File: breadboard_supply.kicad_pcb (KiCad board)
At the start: 4 copper layers, 54 x 100 mm, 187 parts, among them J1 USB_C_Receptacle_USB2.0, J2 Barrel_Jack_Switch, J3 ST-Link, J4 SHDN, J5 SHDN, J6 RAIL_POL, J7 OUTPUT, J8 RAIL_POL, J9 OUTPUT, K1 HFD4-3, K2 HFD4-3, Q1 AO4805, Q2 AO4805, Q3 DMG2302U, Q4 AO4805, Q5 DMG2302U, Q6 DMG2302U, SW1 Button, SW2 Button, SW3 Button, SW4 Button, SW5 Button, U1 USBLC6-2SC6, U10 MAX5400, U11 SL6206-33NR, U12 STM32F070RBT6, U13 GN1640T, U14 74LVC1G14, U15 74LVC1G14, U16 INA180A4, U17 INA180A4, U2 CYPD3177-24LQXQ, U3 DZDH0401DW, U4 INA180A4, U5 DZDH0401DW, U6 TPS54202DDC, U7 TPS54202DDC, U8 MAX5400, U9 TPS54202DDC, Y1 8MHz

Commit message: WIP PCB Routing
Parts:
- L1, L2, L3: footprint Inductor_SMD:L_6.3x6.3_H3 -> Inductor_SMD:L_Bourns_SRN6045TA
- R50: moved to B.Cu
- moved R30 228.8 mm to (18.6, 120.6)
- moved C18 217.0 mm to (21.5, 124.4)
- moved R32 212.3 mm to (32.2, 119.2)
- moved R31 210.1 mm to (24.8, 127.9)
- moved U7 208.1 mm to (19.3, 109.8)
- moved C15 201.7 mm to (28.5, 125.3)
- moved C17 198.7 mm to (25.5, 114.9)
- moved U8 198.3 mm to (25.6, 120.1)
- moved C20 193.8 mm to (32.7, 109.4)
- moved C21 191.0 mm to (32.9, 115.5)
- moved R33 189.9 mm to (32.3, 122.6)
- moved C19 186.5 mm to (19.5, 115.4)
- moved C16 184.9 mm to (25.6, 109.5)
- moved L2 180.4 mm to (26.4, 101.1)
- moved R28 173.8 mm to (67.5, 22.4)
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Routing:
- net Net-(C25-Pad2): track 0.00 -> 22.9 mm
- net Net-(K2-Pad3): track 18.6 -> 6.06 mm
- net Net-(K1-Pad3): track 16.0 -> 6.06 mm
- net Net-(Q6-Pad1): track 12.9 -> 4.52 mm
- net Net-(C22-Pad2): track 0.00 -> 7.01 mm, vias 0 -> 8
- net GND: track 40.4 -> 46.1 mm, vias 19 -> 27
- net Net-(R37-Pad2): track 0.00 -> 5.27 mm
- net /Buck Converter/BUCK_EN_RIGHT: track 0.00 -> 3.33 mm, vias 0 -> 1
- net +3.3V: track 20.5 -> 23.6 mm
- net Net-(R36-Pad2): track 0.00 -> 2.75 mm
- net Net-(C22-Pad1): track 0.00 -> 2.62 mm
- net /Buck Converter/DP_DIN: track 0.00 -> 1.99 mm, vias 0 -> 1
- net Net-(Q5-Pad1): track 4.02 -> 2.33 mm
- net /Buck Converter/~{DP_CS_RIGHT}: track 0.00 -> 1.58 mm, vias 0 -> 1
- net /Buck Converter/DP_SCLK: track 0.00 -> 1.58 mm, vias 0 -> 1
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- added copper zone on F.Cu, net GND
- added copper zone on B.Cu, net Net-(C22-Pad2)
- added copper zone on F.Cu, net Net-(C22-Pad2)
- added copper zone on F.Cu, net Net-(K1-Pad3)
- added copper zone on F.Cu, net Net-(K2-Pad3)
- added copper zone on F.Cu, net VCC
- added copper zone on F.Cu, net VEE
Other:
- board text added: "A"
- board text added: "DSP"
- board text added: "ON"
- board text added: "V"
- board text added: "WARN"

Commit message: Add mounting holes, WIP routing
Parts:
- removed R48, R49, R50, R51, R52: 10K, Resistor_SMD:R_0603_1608Metric
- added H1: MountingHole, MountingHole:MountingHole_3.2mm_M3_Pad, F.Cu at (43.3, 44.0)
- added H2: MountingHole, MountingHole:MountingHole_3.2mm_M3_Pad, F.Cu at (89.2, 44.0)
- C43, C44, U13: moved to B.Cu
- R59, R67: moved to F.Cu
- moved C44 129.1 mm to (60.2, 106.3), turned to 180 degrees
- moved C43 127.6 mm to (64.4, 107.1)
- moved U13 106.7 mm to (59.9, 101.6), turned to -90 degrees
- moved R59 73.7 mm to (114.2, 86.4), turned to 0 degrees
- moved R44 64.3 mm to (111.3, 79.3)
- moved C42 64.3 mm to (102.1, 78.9)
- moved R41 64.3 mm to (98.0, 78.7)
- moved R45 64.3 mm to (111.6, 75.7)
- moved C41 64.3 mm to (102.5, 75.8)
- moved R40 64.3 mm to (98.3, 75.7)
- moved R31 56.9 mm to (49.3, 76.6), turned to 180 degrees
- moved C15 49.5 mm to (47.5, 79.6), turned to -90 degrees
- moved R33 49.3 mm to (44.9, 74.9), turned to 180 degrees
- moved C18 47.5 mm to (40.6, 80.9), turned to 90 degrees
- moved R32 47.5 mm to (49.3, 74.9), turned to 180 degrees
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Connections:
- D10 pad 1: /User Interface/GR7 -> /User Interface/GR10
- D10 pad 2: /User Interface/SEG6 -> /User Interface/SEG1
- D11 pad 1: /User Interface/GR7 -> /User Interface/GR10
- D11 pad 2: /User Interface/SEG7 -> /User Interface/SEG3
- D12 pad 1: /User Interface/GR7 -> /User Interface/GR10
- D12 pad 2: /User Interface/SEG8 -> /User Interface/SEG7
- D5 pad 1: /User Interface/GR7 -> /User Interface/GR10
- D5 pad 2: /User Interface/SEG1 -> /User Interface/SEG5
- D6 pad 1: /User Interface/GR7 -> /User Interface/GR10
- D6 pad 2: /User Interface/SEG2 -> /User Interface/SEG4
- D7 pad 1: /User Interface/GR7 -> /User Interface/GR10
- D7 pad 2: /User Interface/SEG3 -> /User Interface/SEG6
- D8 pad 1: /User Interface/GR7 -> /User Interface/GR10
- D8 pad 2: /User Interface/SEG4 -> /User Interface/SEG8
- D9 pad 1: /User Interface/GR7 -> /User Interface/GR10
- D9 pad 2: /User Interface/SEG5 -> /User Interface/SEG2
- LED1 pad 12: /User Interface/GR1 -> /User Interface/GR11
- LED1 pad 8: /User Interface/GR3 -> /User Interface/GR15
- LED1 pad 9: /User Interface/GR2 -> /User Interface/GR13
- LED2 pad 12: /User Interface/GR4 -> /User Interface/GR12
- LED2 pad 8: /User Interface/GR6 -> /User Interface/GR16
- LED2 pad 9: /User Interface/GR5 -> /User Interface/GR14
- U13 pad 1: unconnected-(U13-Pad1) -> /User Interface/GR12
- U13 pad 18: /User Interface/GR1 -> unconnected-(U13-Pad18)
- U13 pad 19: /User Interface/GR2 -> unconnected-(U13-Pad19)
- U13 pad 2: unconnected-(U13-Pad2) -> /User Interface/GR13
- U13 pad 20: /User Interface/GR3 -> unconnected-(U13-Pad20)
- U13 pad 21: /User Interface/GR4 -> unconnected-(U13-Pad21)
- U13 pad 22: /User Interface/GR5 -> unconnected-(U13-Pad22)
- U13 pad 23: /User Interface/GR6 -> unconnected-(U13-Pad23)
- U13 pad 24: /User Interface/GR7 -> unconnected-(U13-Pad24)
- U13 pad 27: unconnected-(U13-Pad27) -> /User Interface/GR10
- U13 pad 28: unconnected-(U13-Pad28) -> /User Interface/GR11
- U13 pad 3: unconnected-(U13-Pad3) -> /User Interface/GR14
- U13 pad 4: unconnected-(U13-Pad4) -> /User Interface/GR15
- U13 pad 5: unconnected-(U13-Pad5) -> /User Interface/GR16
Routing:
- net /User Interface/SEG2: track 0.00 -> 47.3 mm, vias 0 -> 1
- net /User Interface/GR10: track 0.00 -> 46.5 mm, vias 0 -> 1
- net /User Interface/SEG1: track 0.00 -> 38.1 mm, vias 0 -> 1
- net VCC: track 0.00 -> 35.4 mm, vias 0 -> 25
- net /User Interface/GR15: track 0.00 -> 35.1 mm
- net /User Interface/GR13: track 0.00 -> 33.7 mm
- net /User Interface/GR11: track 0.00 -> 32.3 mm
- net /User Interface/SEG7: track 0.00 -> 31.1 mm, vias 0 -> 1
- net VDD: track 0.00 -> 30.7 mm
- net /User Interface/SEG3: track 0.00 -> 30.0 mm, vias 0 -> 1
- net /User Interface/SEG6: track 0.00 -> 28.8 mm, vias 0 -> 1
- net Net-(D16-Pad1): track 0.00 -> 27.2 mm, vias 0 -> 2
- net Net-(D17-Pad1): track 0.00 -> 26.5 mm, vias 0 -> 2
- net /User Interface/SEG5: track 0.00 -> 25.9 mm
- net /User Interface/SEG8: track 0.00 -> 25.8 mm, vias 0 -> 1
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- added copper zone on B.Cu, net +3.3V
- added copper zone on B.Cu, net GND
- added copper zone on B.Cu, net Net-(C15-Pad2)
- added copper zone on F.Cu, net Net-(C15-Pad2)
- added copper zone on B.Cu, net VCC
- added copper zone on F.Cu, net VDD
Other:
- board text added: "RD"
- board text added: "WR"
- board text removed: "WARN"

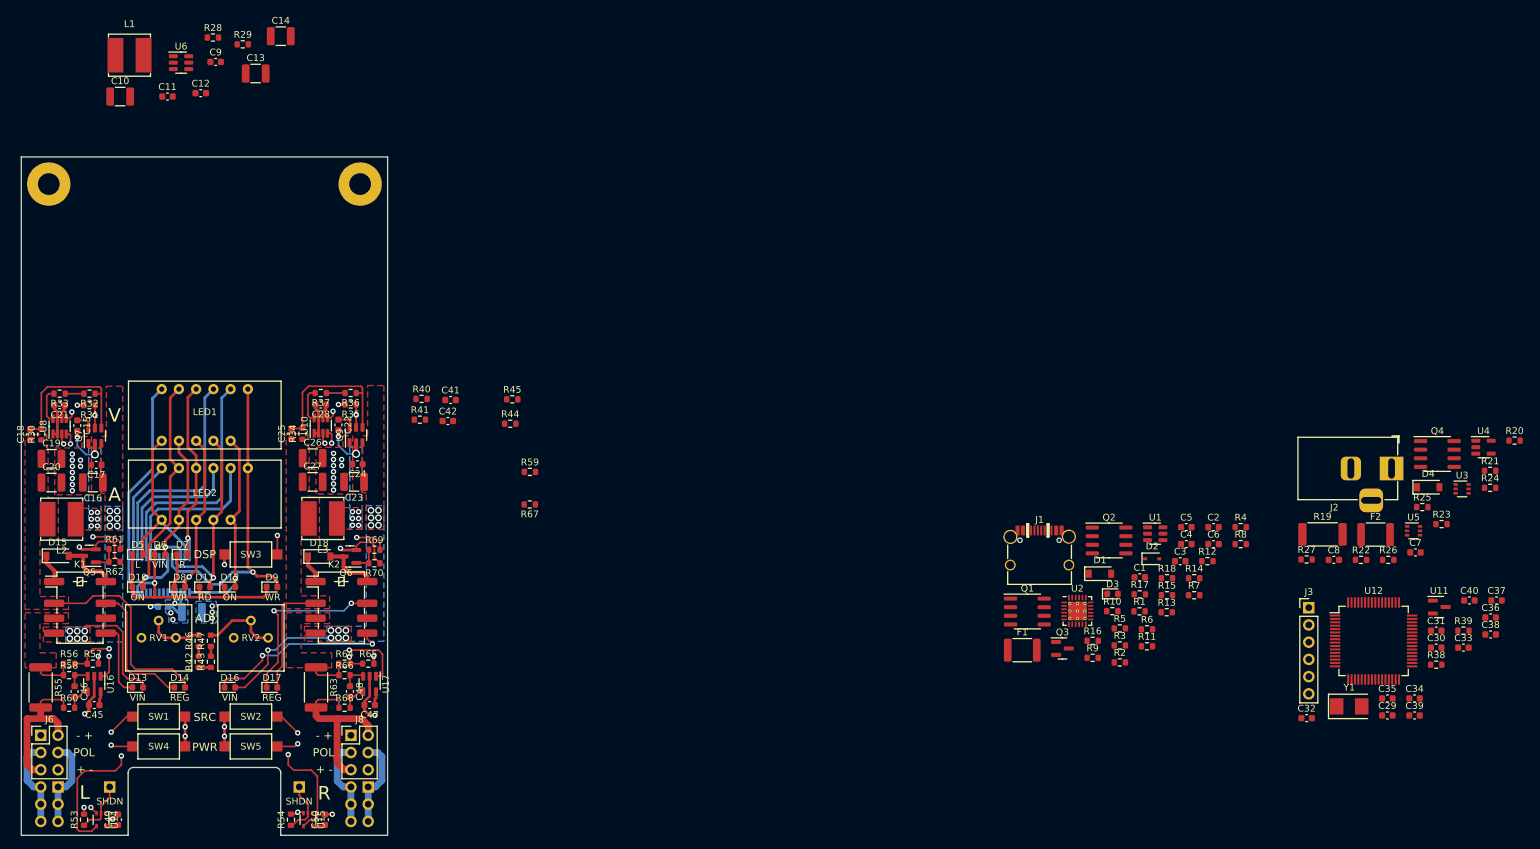
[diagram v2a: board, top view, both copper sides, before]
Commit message: WIP PCB routing
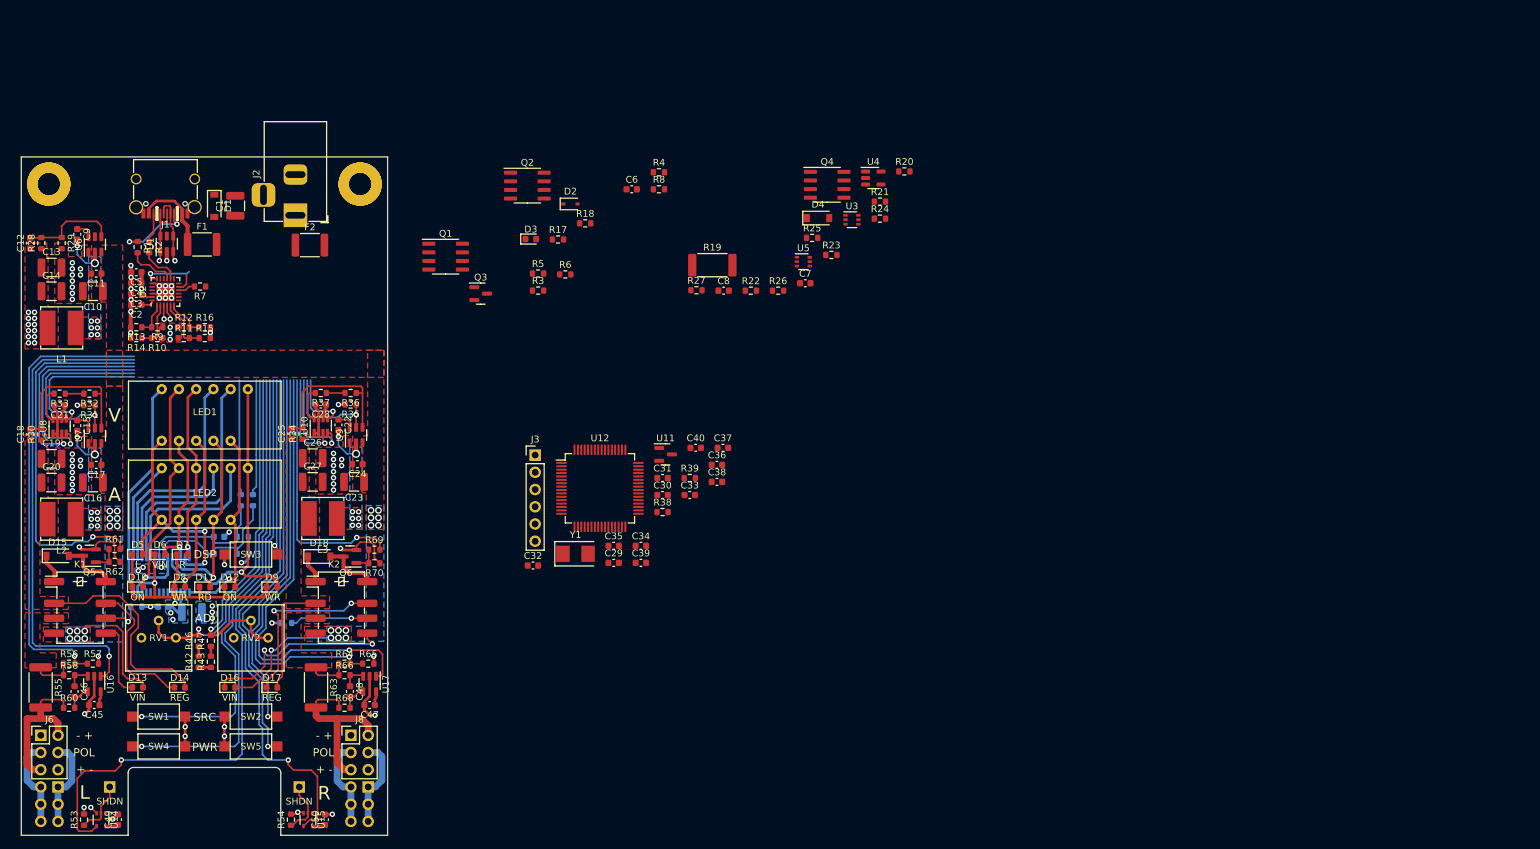
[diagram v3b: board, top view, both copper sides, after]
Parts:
- added H1: MountingHole_Pad, MountingHole:MountingHole_3.2mm_M3_Pad, F.Cu at (43.3, 44.0)
- added H2: MountingHole_Pad, MountingHole:MountingHole_3.2mm_M3_Pad, F.Cu at (89.2, 44.0)
- C1: footprint Capacitor_SMD:C_0603_1608Metric -> Capacitor_SMD:C_1210_3225Metric
- C41, C42, R40, R41, R44, R45, R59, R67: moved to B.Cu
- U2: footprint Package_DFN_QFN:QFN-24-1EP_4x4mm_P0.5mm_EP2.7x2.7mm_ThermalVias -> Package_DFN_QFN:QFN-24-1EP_4x4mm_P0.5mm_EP2.7x2.7mm
- moved J2 165.8 mm to (79.7, 48.6), turned to -90 degrees
- moved F2 162.8 mm to (81.8, 53.0)
- moved C2 162.1 mm to (56.2, 61.8), turned to 180 degrees
- moved R14 159.9 mm to (56.2, 66.7), turned to 180 degrees
- moved C4 159.5 mm to (56.2, 58.6), turned to 180 degrees
- moved C5 159.3 mm to (56.2, 57.0), turned to 180 degrees
- moved C3 158.9 mm to (56.2, 60.2), turned to 180 degrees
- moved R13 157.6 mm to (56.2, 65.1), turned to 180 degrees
- moved R1 157.1 mm to (56.4, 53.3), turned to -90 degrees
- moved R2 155.6 mm to (58.1, 53.3), turned to -90 degrees
- moved R12 154.8 mm to (63.2, 65.1)
- moved R7 153.5 mm to (65.6, 59.1), turned to 180 degrees
- moved U1 151.8 mm to (60.7, 52.8), turned to 90 degrees
- moved R11 149.1 mm to (63.2, 66.7)
- moved R15 146.8 mm to (66.3, 66.7)
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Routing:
- net /Microcontroller/~{SHDN_LEFT}: track 19.4 -> 94.7 mm
- net /Microcontroller/BTN_ON_LEFT: track 3.18 -> 72.9 mm
- net /Microcontroller/ISENSE_LEFT: track 3.81 -> 72.4 mm
- net /Microcontroller/BTN_SEL_LEFT: track 4.19 -> 68.0 mm
- net /Microcontroller/~{SHDN_RIGHT}: track 15.1 -> 77.5 mm
- net /Microcontroller/VSENSE_LEFT: track 6.79 -> 67.7 mm
- net /Microcontroller/VSENSE_RIGHT: track 2.90 -> 60.6 mm
- net /Microcontroller/ISENSE_RIGHT: track 9.13 -> 66.0 mm
- net /Microcontroller/BTN_ON_RIGHT: track 3.17 -> 59.4 mm
- net /Microcontroller/BTN_SEL_RIGHT: track 3.99 -> 54.1 mm
- net /Microcontroller/RELAY_LEFT: track 5.37 -> 54.5 mm
- net /Microcontroller/POT_LEFT: track 8.14 -> 52.4 mm, vias 0 -> 1
- net /Microcontroller/POT_RIGHT: track 11.4 -> 52.1 mm, vias 0 -> 1
- net /Buck Converter/DP_DIN: track 3.98 -> 44.5 mm
- net /Microcontroller/RELAY_RIGHT: track 4.74 -> 37.6 mm
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- added copper zone on F.Cu, net +3.3V
- added copper zone on F.Cu, net +3.3VP
- added copper zone on B.Cu, net Net-(C9-Pad2)
- added copper zone on F.Cu, net Net-(C9-Pad2)

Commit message: WIP PCb routing
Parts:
- removed C35: 100nF, Capacitor_SMD:C_0603_1608Metric
- removed the H1 at (43.3, 44.0)
- removed the H2 at (89.2, 44.0)
- C29, C30, C31, C32, C33, C34, C36, C39, C40, R38, R39, U12, Y1: moved to B.Cu
- J3: footprint Connector_PinHeader_2.54mm:PinHeader_1x06_P2.54mm_Vertical -> Connector_PinHeader_1.27mm:PinHeader_2x03_P1.27mm_Vertical_SMD; moved to B.Cu
- moved R20 85.3 mm to (86.1, 60.2)
- moved U5 77.7 mm to (76.8, 55.4), turned to 90 degrees
- moved U4 77.7 mm to (89.8, 63.2), turned to -90 degrees
- moved Q4 77.5 mm to (81.3, 54.8), turned to 90 degrees
- moved R21 77.4 mm to (89.6, 60.2)
- moved C30 76.3 mm to (66.3, 54.3), turned to 180 degrees
- moved R24 76.1 mm to (90.0, 55.6)
- moved U3 75.2 mm to (86.8, 56.4), turned to 90 degrees
- moved R26 74.7 mm to (76.1, 58.7), turned to -90 degrees
- moved R23 73.6 mm to (86.1, 66.7)
- moved R39 71.8 mm to (75.6, 51.4), turned to 90 degrees
- moved R18 71.4 mm to (51.2, 44.4), turned to 180 degrees
- moved C38 70.0 mm to (77.0, 61.4)
- moved C37 66.7 mm to (77.8, 67.4)
- moved C29 66.5 mm to (68.3, 67.9), turned to -90 degrees
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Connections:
- net Net-(Q4-Pad1) renamed /Power Input/PWRIN
- C29 pad 1: +3V3 -> +3.3V
- C30 pad 1: +3V3 -> +3.3V
- C31 pad 1: +3V3 -> +3.3V
- C32 pad 1: +3V3 -> +3.3V
- C33 pad 1: +3V3 -> +3.3V
- C34 pad 1: +3V3 -> +3.3V
- C38 pad 1: +3V3 -> +3.3V
- J3 pad 1: +3V3 -> /Microcontroller/SWO
- J3 pad 2: /Microcontroller/SWCLK -> +3.3V
- J3 pad 3: GND -> /Microcontroller/SWCLK
- J3 pad 4: /Microcontroller/SWDIO -> GND
- J3 pad 6: /Microcontroller/SWO -> /Microcontroller/SWDIO
- Q4 pad 5: VCCQ -> /Power Input/VIN
- Q4 pad 6: VCCQ -> /Power Input/VIN
- Q4 pad 7: /Power Input/VIN -> VCCQ
- Q4 pad 8: /Power Input/VIN -> VCCQ
- R25 pad 1: Net-(Q4-Pad2) -> Net-(Q4-Pad4)
- R27 pad 1: Net-(Q4-Pad4) -> Net-(Q4-Pad2)
- R38 pad 1: +3V3 -> +3.3V
- SW3 pad 2: /User Interface/BTN_SEL_MEAS -> /Microcontroller/BTN_SEL_MEAS
- U11 pad 2: +3V3 -> +3.3V
- U12 pad 1: +3V3 -> +3.3V
- U12 pad 10: /Microcontroller/POT_RIGHT -> /Microcontroller/POT_LEFT
- U12 pad 11: /Microcontroller/ISENSE_VIN -> /Microcontroller/POT_RIGHT
- U12 pad 13: +3V3 -> +3.3V
- U12 pad 14: /Microcontroller/ISENSE_LEFT -> /Microcontroller/VSENSE_VIN
- U12 pad 15: /Microcontroller/VSENSE_LEFT -> /Microcontroller/ISENSE_VIN
- U12 pad 16: /Microcontroller/POT_LEFT -> /Microcontroller/ISENSE_RIGHT
- U12 pad 17: /Microcontroller/VSENSE_VIN -> /Microcontroller/VSENSE_RIGHT
- U12 pad 19: +3V3 -> +3.3V
- U12 pad 2: /Microcontroller/BTN_SEL_MEAS -> /Buck Converter/~{DP_CS_RIGHT}
- U12 pad 20: /Microcontroller/~{SHDN_LEFT} -> unconnected-(U12-Pad20)
- U12 pad 24: /Microcontroller/~{SHDN_RIGHT} -> /Microcontroller/BTN_SEL_RIGHT
- U12 pad 25: unconnected-(U12-Pad25) -> /Microcontroller/BTN_ON_RIGHT
- U12 pad 26: /Microcontroller/PD_FAULT -> /Microcontroller/~{SHDN_RIGHT}
- U12 pad 27: /Buck Converter/BUCK_EN_LEFT -> /Microcontroller/BTN_SEL_MEAS
- U12 pad 28: /Microcontroller/RELAY_LEFT -> /Microcontroller/~{SHDN_LEFT}
- U12 pad 29: unconnected-(U12-Pad29) -> /Microcontroller/BTN_ON_LEFT
- U12 pad 3: /Microcontroller/BTN_ON_LEFT -> /Buck Converter/BUCK_EN_RIGHT
- U12 pad 30: unconnected-(U12-Pad30) -> /Microcontroller/BTN_SEL_LEFT
- U12 pad 32: +3V3 -> +3.3V
- U12 pad 4: /Microcontroller/BTN_ON_RIGHT -> /Microcontroller/RELAY_RIGHT
- U12 pad 40: unconnected-(U12-Pad40) -> /Buck Converter/BUCK_EN_LEFT
- U12 pad 42: /Buck Converter/~{DP_CS_RIGHT} -> /Microcontroller/RELAY_LEFT
- U12 pad 43: unconnected-(U12-Pad43) -> /Microcontroller/PD_FAULT
- U12 pad 48: +3V3 -> +3.3V
- U12 pad 52: /Microcontroller/BTN_SEL_LEFT -> unconnected-(U12-Pad52)
- U12 pad 53: /Microcontroller/BTN_SEL_RIGHT -> unconnected-(U12-Pad53)
- U12 pad 61: /Buck Converter/BUCK_EN_RIGHT -> unconnected-(U12-Pad61)
- U12 pad 62: /Microcontroller/RELAY_RIGHT -> unconnected-(U12-Pad62)
- U12 pad 64: +3V3 -> +3.3V
- U12 pad 8: /Microcontroller/ISENSE_RIGHT -> /Microcontroller/VSENSE_LEFT
- U12 pad 9: /Microcontroller/VSENSE_RIGHT -> /Microcontroller/ISENSE_LEFT
- U3 pad 3: Net-(Q4-Pad2) -> Net-(Q4-Pad4)
- U5 pad 3: Net-(Q4-Pad4) -> Net-(Q4-Pad2)
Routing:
- net GND: track 87.3 -> 150.0 mm, vias 71 -> 89
- net VBUS: track 7.43 -> 61.4 mm, vias 1 -> 2
- net /Buck Converter/DP_SCLK: track 31.2 -> 82.6 mm, vias 2 -> 4
- net +3.3V: track 32.2 -> 79.7 mm, vias 16 -> 39
- net /Microcontroller/RELAY_RIGHT: track 37.6 -> 81.8 mm
- net /Buck Converter/DP_DIN: track 44.5 -> 86.8 mm, vias 2 -> 6
- net /Buck Converter/~{DP_CS_RIGHT}: track 13.9 -> 52.3 mm
- net /Microcontroller/BTN_SEL_MEAS: track 0.00 -> 34.7 mm, vias 0 -> 1
- net /Buck Converter/BUCK_EN_RIGHT: track 15.9 -> 46.7 mm
- net /Microcontroller/VSENSE_LEFT: track 67.7 -> 96.3 mm, vias 1 -> 3
- net /Microcontroller/PD_FAULT: track 0.00 -> 28.3 mm, vias 0 -> 2
- net /Microcontroller/ISENSE_LEFT: track 72.4 -> 100.5 mm, vias 1 -> 3
- net /User Interface/BTN_SEL_MEAS: track 26.0 -> 0.00 mm, vias 1 -> 0
- net /Microcontroller/NRST: track 0.00 -> 24.5 mm
- net VCCQ: track 2.62 -> 27.1 mm, vias 0 -> 2
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- added copper zone on In2.Cu, net +3.3V
- added copper zone on B.Cu, net +3.3VP
- added copper zone on F.Cu, net /Power Input/PWRIN
- added copper zone on F.Cu, net /Power Input/VIN
- added copper zone on F.Cu, net Net-(F2-Pad1)
- added copper zone on F.Cu, net VBUS
- added copper zone on F.Cu, net VCCQ
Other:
- board text added: "24V MAX PD/VIN"
- board text added: "2A Max Per Rail!"
- board text added: "Dual BB Supply"
- board text added: "IO GND 3V3"
- board text added: "PD FAULT"
- board text added: "RST CLK SWO"
- board text added: "Rev 1"
- board text added: "ST-Link"
- board text added: "sleepyponylabs.com"

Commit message: Add information and BOM consolidation for JLCPCB
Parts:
- added G***: LOGO, slp_logo:sleepylogo_10mm, F.Cu at (43.9, 71.1)
- D2: value ZMM12V -> BZT52C12S
- F1, F2: value JK-MSMD200-24V -> ASMD1812-200-30V
- R7: value 4K7 -> 3K3
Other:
- board text added: "2A Max Per Rail"
- board text removed: "2A Max Per Rail!"
